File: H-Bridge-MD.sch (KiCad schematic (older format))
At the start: 67 parts, among them IC1 SI8650AB-B-IS1, IC2 A3921KLPTR-T, IC3 SI8650AB-B-IS1, IC4 A3921KLPTR-T, J1 Conn_01x02, J2 Conn_01x03, J3 Conn_01x05, J4 Conn_01x02, J5 Bus_mechaken_PCIexpress_x16_1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, Q1 NVMFD5C446NT1G, Q2 NVMFD5C446NT1G, Q3 NVMFD5C446NT1G, Q4 NVMFD5C446NT1G, U1 LDL1117S33TR_SOT223-4, U2 STM32F042K6Tx, U3 MCP2562-E-SN, U4 LDL1117S33TR_SOT223-4

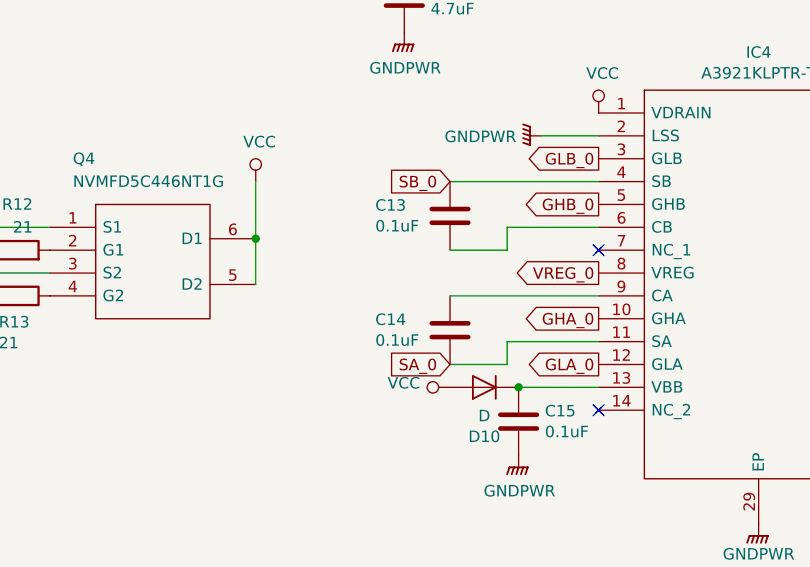
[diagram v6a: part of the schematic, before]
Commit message: change
Bootstrap Capacitor 0.1uF -> 4.4uF
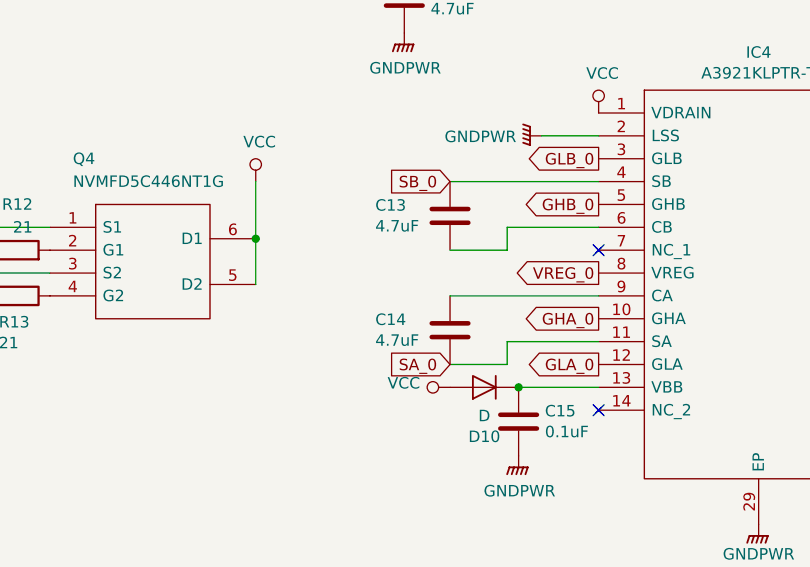
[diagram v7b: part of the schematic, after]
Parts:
- C13, C14: value 0.1uF -> 4.7uF
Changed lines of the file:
@@
 P 11250 6200
 F 0 "C13" H 10923 6246 50  0000 L CNN
-F 1 "0.1uF" H 10923 6155 50  0000 L CNN
+F 1 "4.7uF" H 10923 6155 50  0000 L CNN
 F 2 "Capacitor_SMD:C_0805_2012Metric" H 11288 6050 50  0001 C CNN
 F 3 "~" H 11250 6200 50  0001 C CNN
@@
 P 11250 6700
 F 0 "C14" H 10923 6746 50  0000 L CNN
-F 1 "0.1uF" H 10923 6655 50  0000 L CNN
+F 1 "4.7uF" H 10923 6655 50  0000 L CNN
 F 2 "Capacitor_SMD:C_0805_2012Metric" H 11288 6550 50  0001 C CNN
 F 3 "~" H 11250 6700 50  0001 C CNN

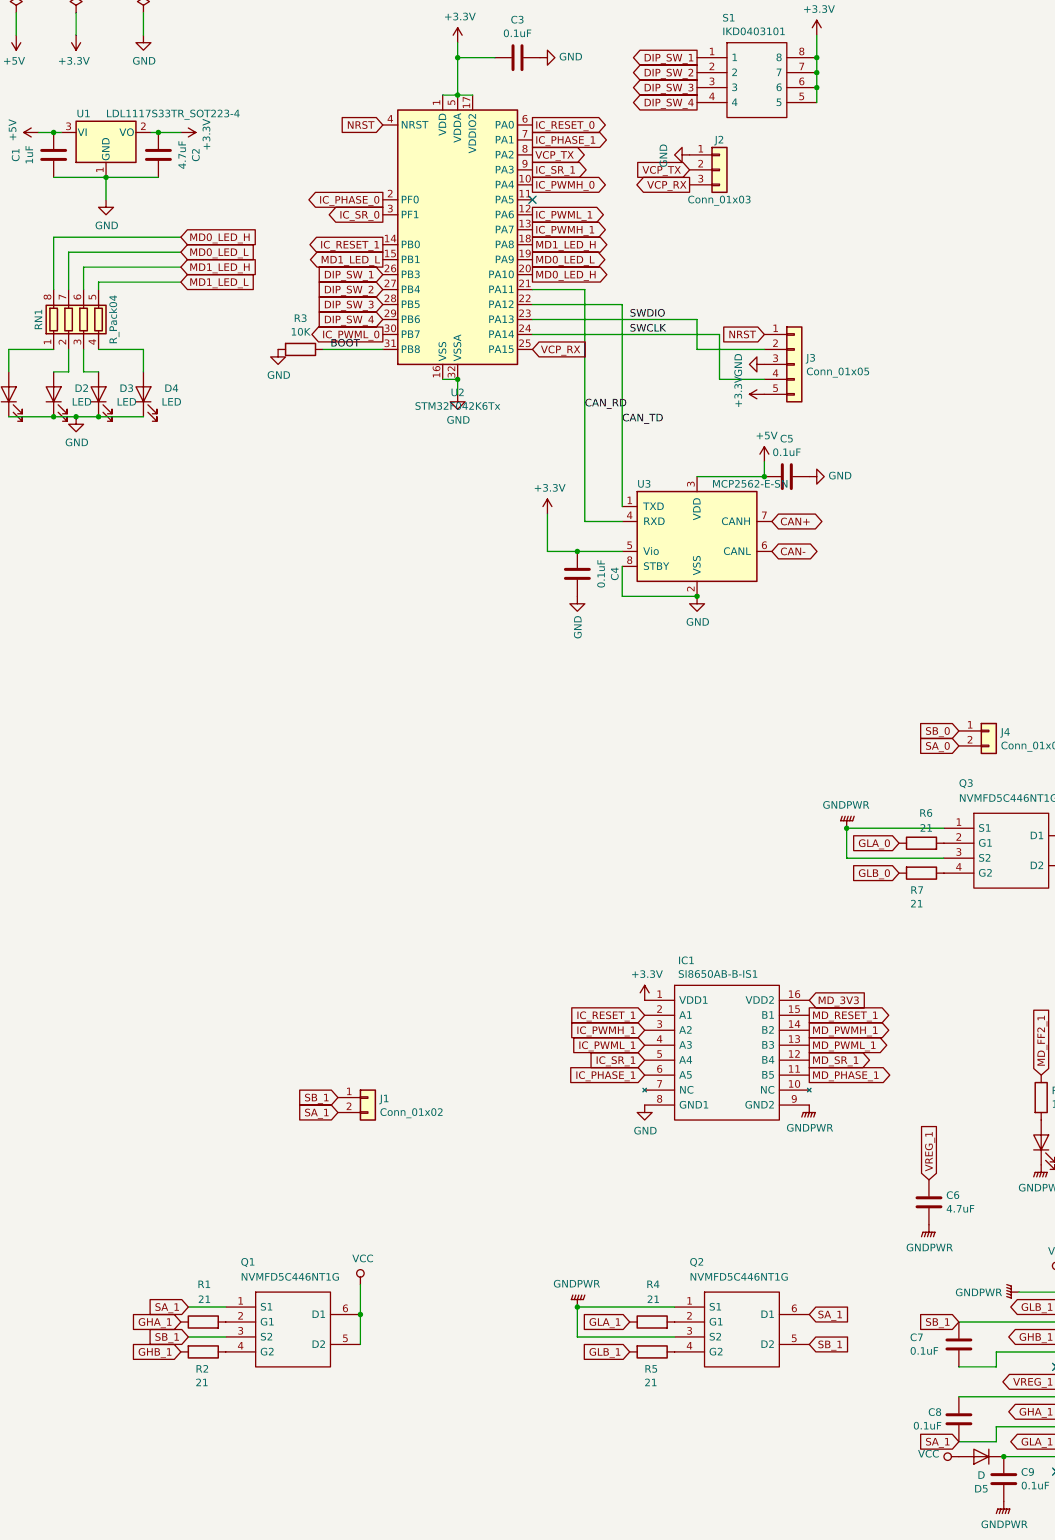
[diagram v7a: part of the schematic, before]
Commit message: fix bootstrap capacitor
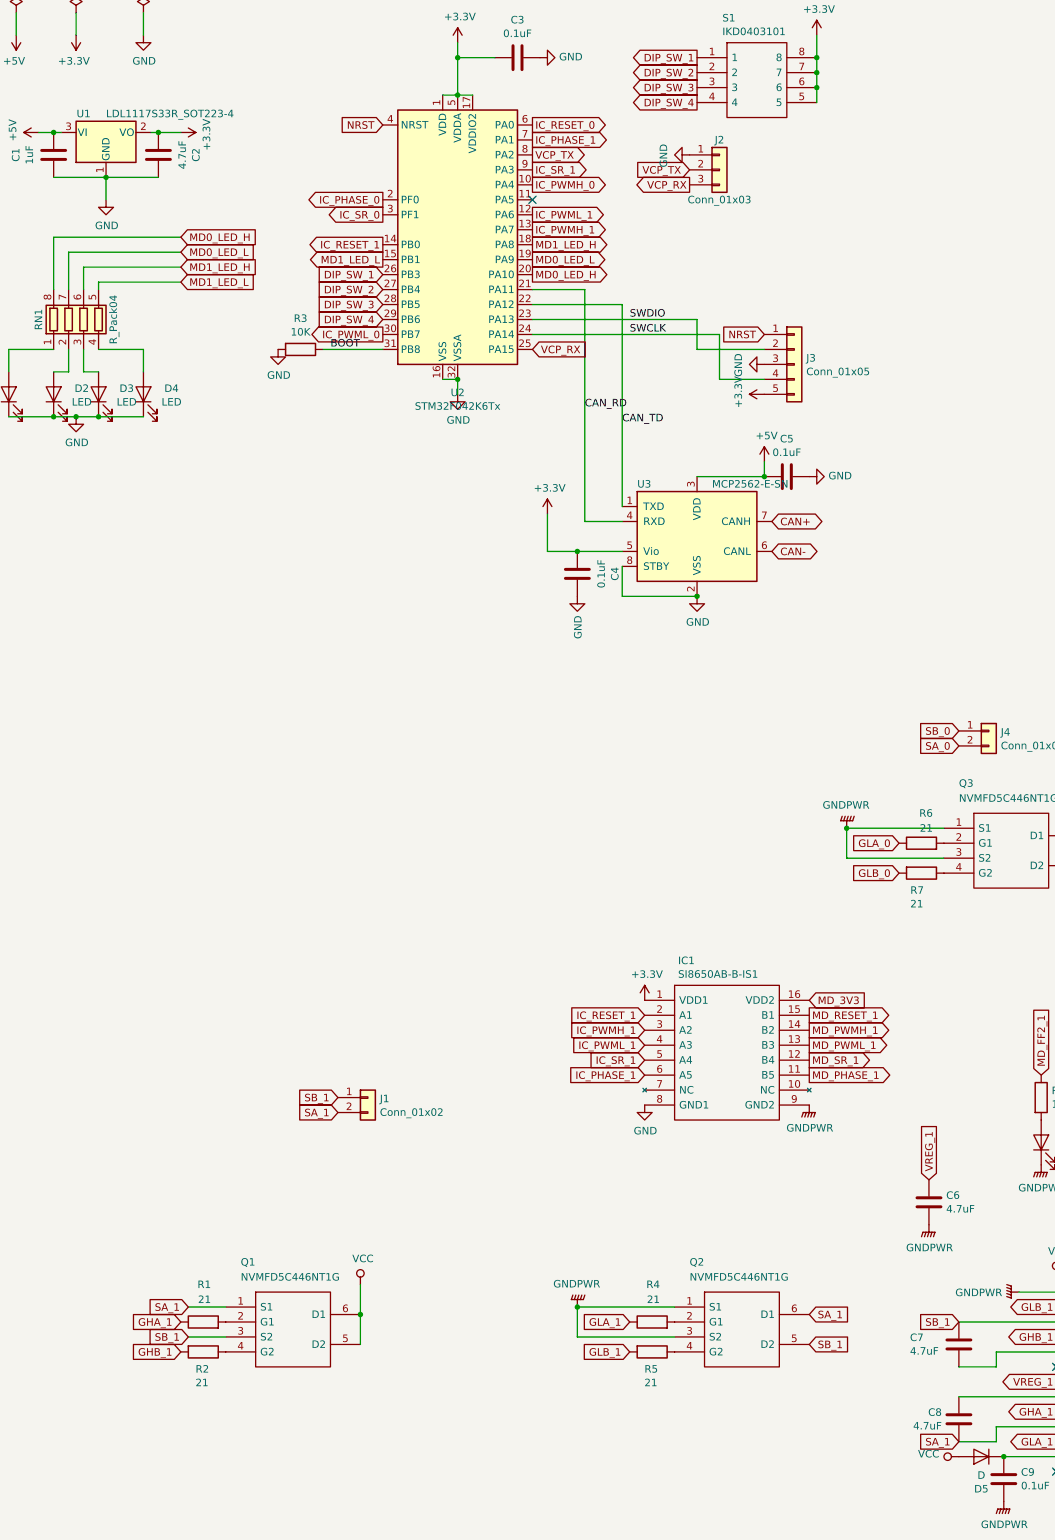
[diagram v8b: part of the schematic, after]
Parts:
- C7, C8: value 0.1uF -> 4.7uF
- U1: value LDL1117S33TR_SOT223-4 -> LDL1117S33R_SOT223-4
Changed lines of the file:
@@
 P 7050 10250
 F 0 "C8" H 7164 10204 50  0000 L CNN
-F 1 "0.1uF" H 7164 10295 50  0000 L CNN
+F 1 "4.7uF" H 7164 10295 50  0000 L CNN
 F 2 "Capacitor_SMD:C_0805_2012Metric" H 7088 10100 50  0001 C CNN
 F 3 "~" H 7050 10250 50  0001 C CNN
@@
 P 7050 9750
 F 0 "C7" H 6723 9796 50  0000 L CNN
-F 1 "0.1uF" H 6723 9705 50  0000 L CNN
+F 1 "4.7uF" H 6723 9705 50  0000 L CNN
 F 2 "Capacitor_SMD:C_0805_2012Metric" H 7088 9600 50  0001 C CNN
 F 3 "~" H 7050 9750 50  0001 C CNN
@@
 P 1350 1650
 F 0 "U1" H 1200 1775 50  0000 C CNN
-F 1 "LDL1117S33TR_SOT223-4" H 1350 1775 50  0000 L CNN
+F 1 "LDL1117S33R_SOT223-4" H 1350 1775 50  0000 L CNN
 F 2 "Package_TO_SOT_SMD:SOT-223-3_TabPin2" H 1350 1850 50  0001 C CNN
 F 3 "http://www.st.com/st-web-ui/static/active/en/resource/technical/document/datasheet/CD00000544.pdf" H 1450 1400 50  0001 C CNN
